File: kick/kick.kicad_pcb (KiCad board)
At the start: 2 copper layers, 106.7 x 50.8 mm, 56 parts, among them J1 CV IN, J3 TRIGGER OUT, Q1 BC546, Q2 BC546, Q3 BC556, Q4 BC546, Q5 BC546, Q6 BC546, U1 TL072P

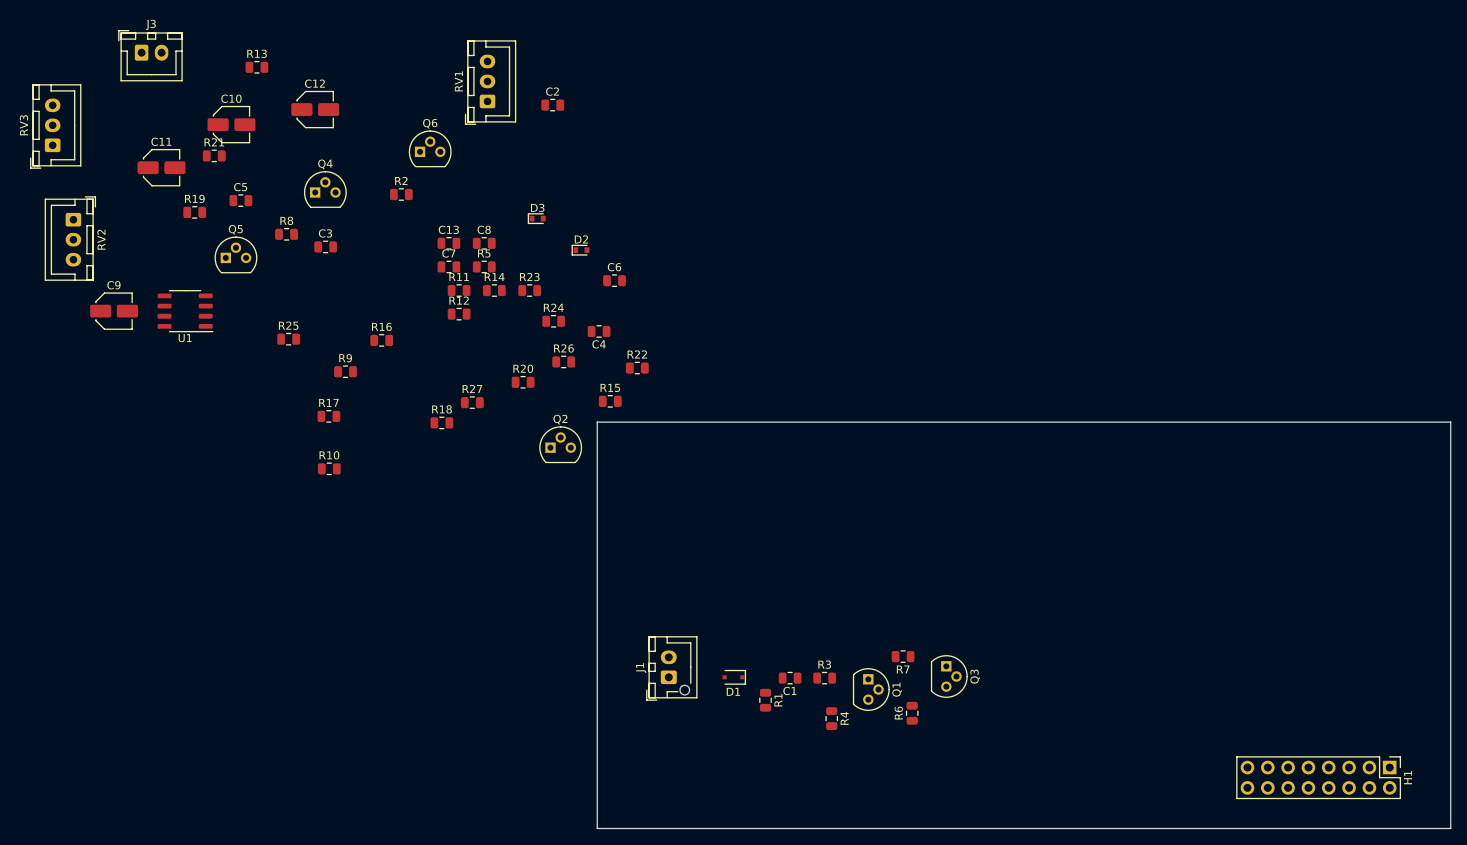
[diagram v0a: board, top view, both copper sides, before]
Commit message: add pcb layout
Signed-off-by: nwesem <niclaswesemann@gmail.com>
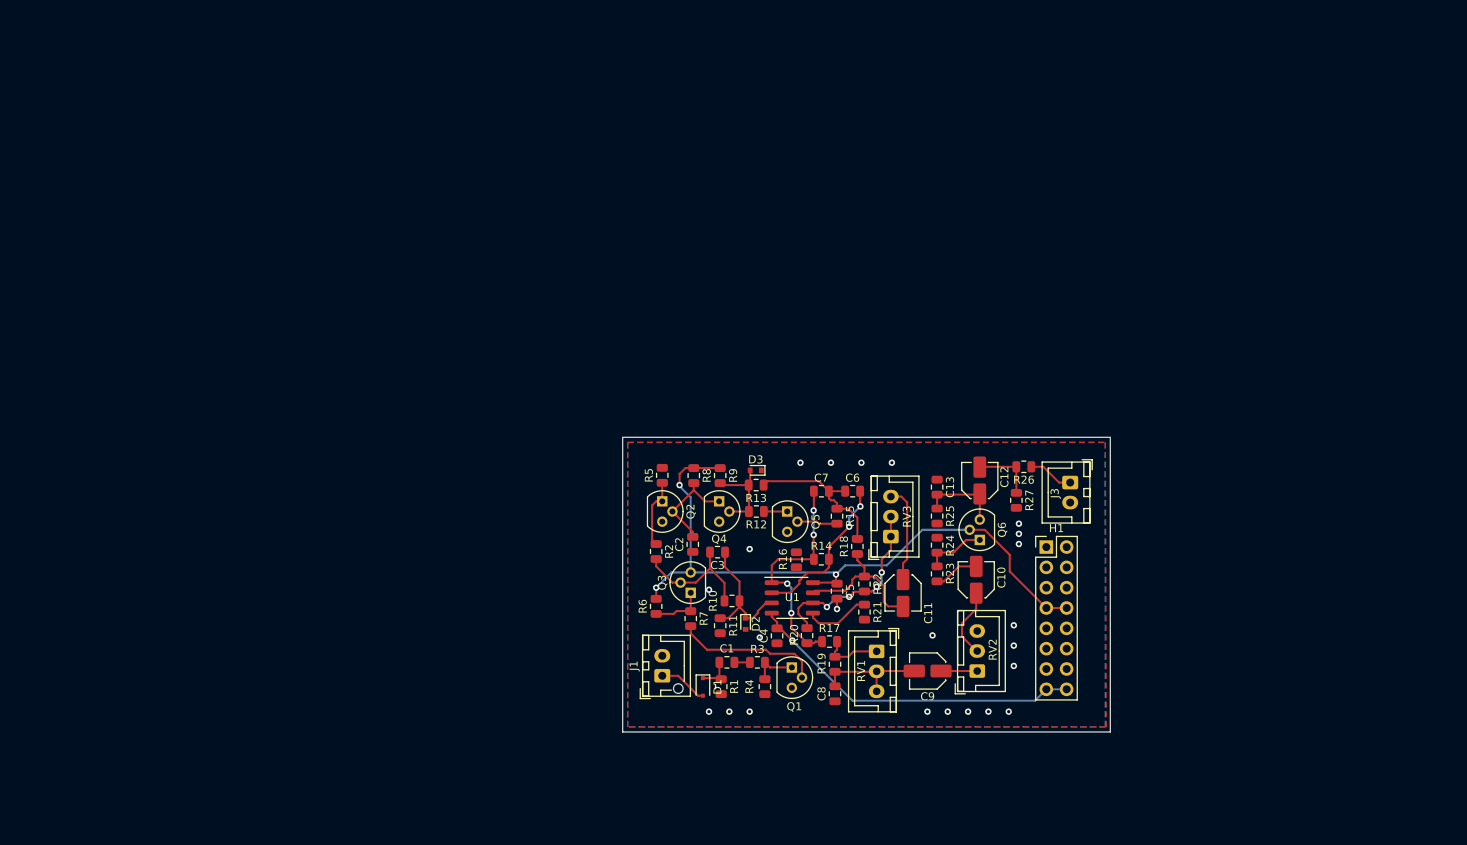
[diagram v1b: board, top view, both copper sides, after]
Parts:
- moved J3 127.9 mm to (163.3, 88.8), turned to 270 degrees
- moved RV2 126.3 mm to (151.6, 112.4), turned to 90 degrees
- moved RV3 115.6 mm to (140.8, 95.6)
- moved C9 111.2 mm to (145.4, 112.4), turned to 180 degrees
- moved C10 109.1 mm to (151.5, 101.0), turned to 90 degrees
- moved C11 106.8 mm to (142.4, 102.6), turned to 270 degrees
- moved R21 99.3 mm to (137.5, 105.0), turned to 270 degrees
- moved R19 98.0 mm to (133.9, 111.6), turned to 270 degrees
- moved C12 95.1 mm to (152.0, 88.6), turned to 90 degrees
- moved C5 89.1 mm to (134.1, 102.4), turned to 270 degrees
- moved Q6 85.1 mm to (152.0, 96.0), turned to 90 degrees
- moved RV1 84.2 mm to (139.1, 109.9), turned to 270 degrees
- moved R25 84.0 mm to (146.6, 93.0), turned to 270 degrees
- moved U1 83.9 mm to (128.5, 103.3), turned to 0 degrees
- moved R13 81.4 mm to (124.0, 89.2), turned to 180 degrees
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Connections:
- U1 pad 4: (no net) -> -12V
- U1 pad 8: (no net) -> +12V
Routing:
- net +12V: track 0.00 -> 83.5 mm, vias 0 -> 3
- net -12V: track 0.00 -> 42.7 mm, vias 0 -> 1
- net Net-(C7-Pad1): track 0.00 -> 28.7 mm, vias 0 -> 4
- net Net-(R20-Pad1): track 0.00 -> 23.8 mm, vias 0 -> 4
- net Net-(C6-Pad2): track 0.00 -> 19.6 mm, vias 0 -> 2
- net Net-(C6-Pad1): track 0.00 -> 19.4 mm
- net Net-(C11-Pad2): track 0.00 -> 18.3 mm
- net Net-(Q1-Pad2): track 0.00 -> 18.3 mm
- net Net-(C3-Pad1): track 0.00 -> 16.5 mm
- net Net-(C3-Pad2): track 0.00 -> 16.1 mm
- net Net-(C8-Pad2): track 0.00 -> 14.3 mm
- net Net-(C2-Pad2): track 0.00 -> 12.6 mm
- net Net-(C11-Pad1): track 0.00 -> 12.2 mm
- net Net-(D3-Pad2): track 0.00 -> 11.3 mm
- net Net-(C12-Pad1): track 0.00 -> 10.3 mm
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- added copper zone on B.Cu, net GND
- added copper zone on F.Cu, net GND
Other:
- board size 106.7 x 50.8 mm -> 61 x 36.8 mm
- net class Default: trace_width 0.25 -> 0.254

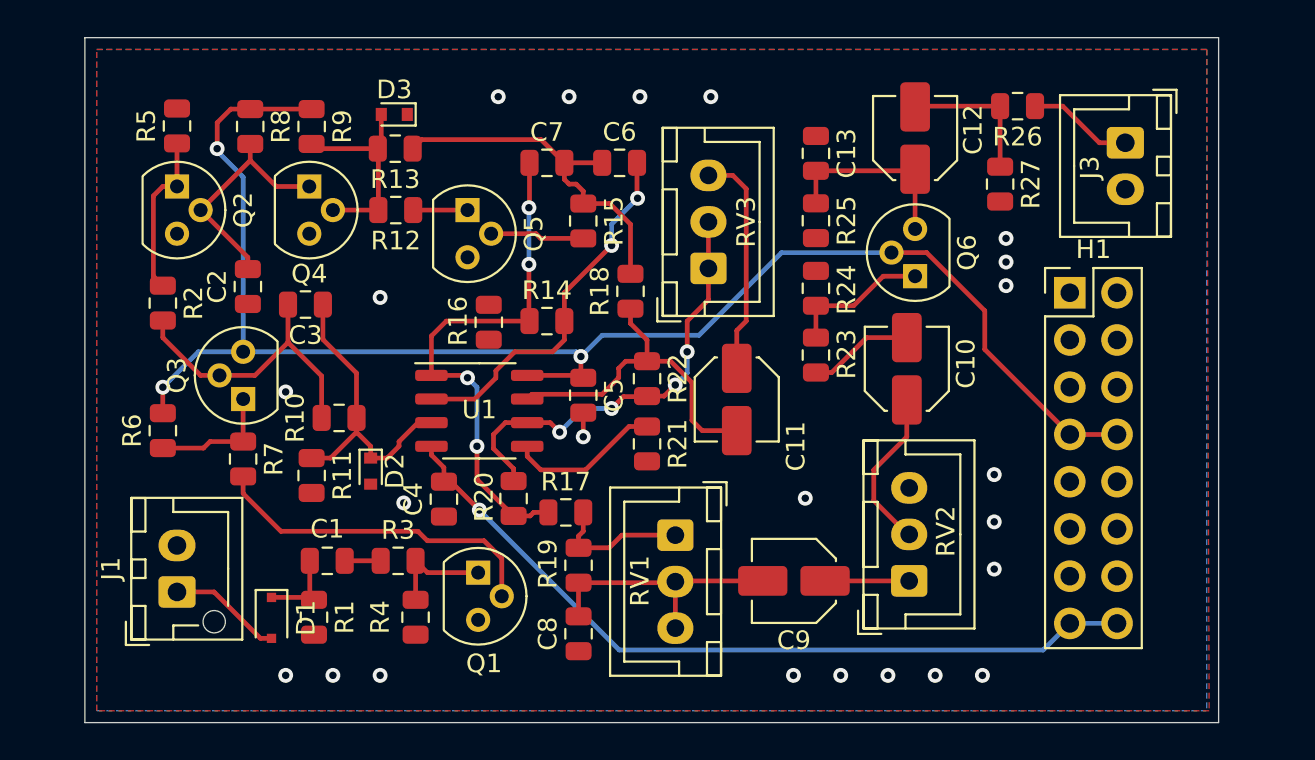
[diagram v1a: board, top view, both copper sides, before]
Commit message: finished kick layout and ordered pcb
Signed-off-by: nwesem <niclaswesemann@gmail.com>
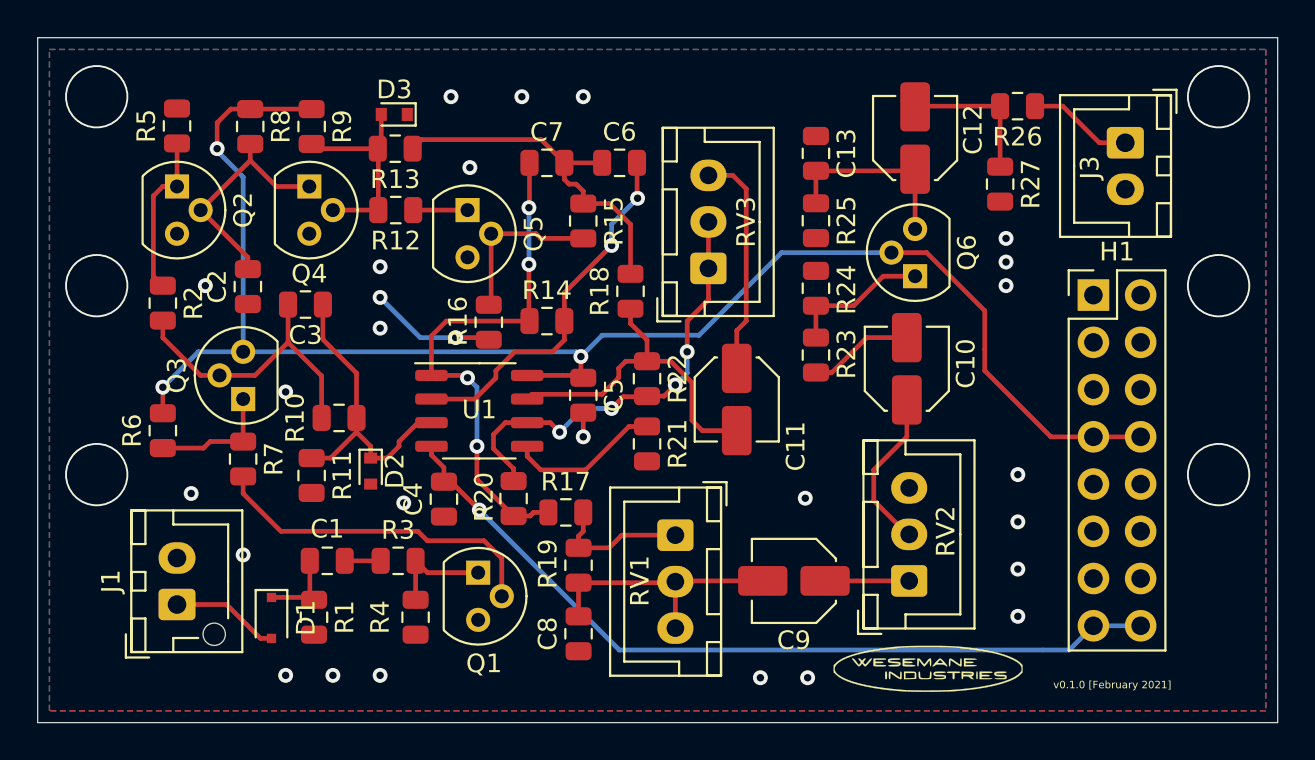
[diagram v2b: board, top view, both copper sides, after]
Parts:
- added G***: LOGO, Logos:wesemane_industries_logo_small, F.Cu at (152.7, 117.2)
- moved H1 1.28 mm to (161.5, 97.0)
- moved J1 0.68 mm to (112.3, 113.7)
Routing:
- net GND: track 1.30 -> 8.15 mm, vias 23 -> 33
- net Net-(Q5-Pad2): track 5.06 -> 8.94 mm
- net +12V: track 83.5 -> 85.5 mm
- net -12V: track 42.7 -> 43.9 mm
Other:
- board size 61 x 36.8 mm -> 66.7 x 36.8 mm
- board text added: "v0.1.0 [February 2021]"
